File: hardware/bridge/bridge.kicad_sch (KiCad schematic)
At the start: 5 parts, among them U1 SIT3088EEUA

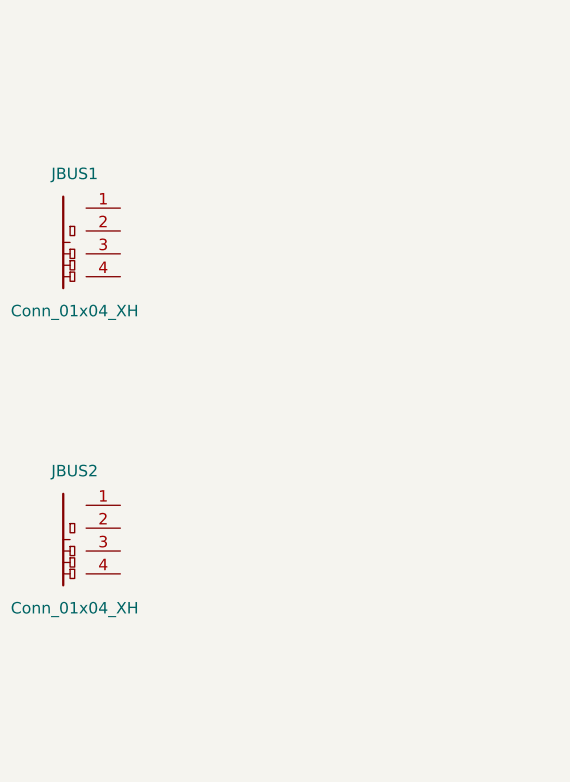
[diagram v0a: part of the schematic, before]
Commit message: hardware: bridge adds DC barrel jacks with reverse-polarity protection
- JDC1, JDC2: JLCPCB C2880546 DC-005K-5A-2.0 barrel jacks (2.0 mm center
  pin, 5.5 mm OD), one per bus connector. Lets the bridge (or any node
  daisy-chained off it) accept a wall-wart input directly instead of
  only bus V+ from another node.
- D1, D2: MBRD10200 Schottky diodes (10 A / 200 V, DPAK, LCSC C260297)
  in series between each DC jack and the corresponding JBUS V+. Protects
  against reverse polarity on the jack and prevents two simultaneously
  plugged jacks from back-feeding each other (diode-OR).

Footprints picked for JLCPCB match:
- DC jack: Connector_BarrelJack:BarrelJack_CUI_PJ-063AH_Horizontal
  (CUI PJ-063AH is 2.0x5.5 mm TH, same electrical spec as DC-005K; close
   mechanical match — verify against datasheet before first fab run)
- Diode:   Package_TO_SOT_SMD:TO-252-2 (DPAK, matches MBRD10200 exactly)

Wiring still pending.
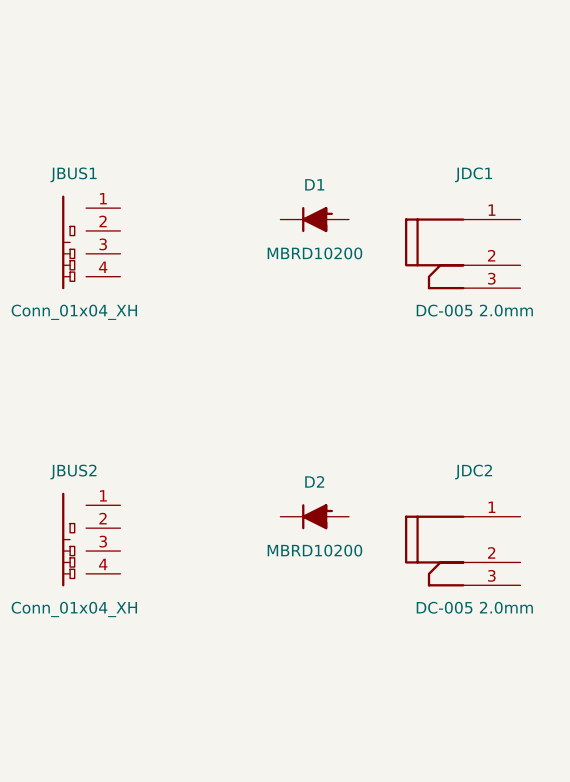
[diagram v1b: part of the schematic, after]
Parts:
- added D1, D2: MBRD10200, Package_TO_SOT_SMD:TO-252-2, symbol Device:D_Schottky
- added JDC1, JDC2: DC-005 2.0mm, Connector_BarrelJack:BarrelJack_CUI_PJ-063AH_Horizontal, symbol Connector:Barrel_Jack_Switch
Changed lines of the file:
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@@
 		(property "Sheetfile" "psu.kicad_sch" (at 25.4 92.0146 0) (effects (font (size 1.27 1.27)) (justify left top)))
+	)
+	(symbol
+		(lib_id "Connector:Barrel_Jack_Switch")
+		(at 228.6 91.44 0)
+		(unit 1)
+		(exclude_from_sim no) (in_bom yes) (on_board yes) (dnp no)
+		(uuid "jdc10001-0000-0000-0000-000000000001")
+		(property "Reference" "JDC1"
+			(at 228.6 83.82 0)
+			(effects (font (size 1.27 1.27)))
+		)
+		(property "Value" "DC-005 2.0mm"
+			(at 228.6 99.06 0)
+			(effects (font (size 1.27 1.27)))
+		)
+		(property "Footprint" "Connector_BarrelJack:BarrelJack_CUI_PJ-063AH_Horizontal"
+			(at 228.6 91.44 0)
+			(effects (font (size 1.27 1.27)) hide)
+		)
+		(property "Datasheet" "~"
+			(at 228.6 91.44 0)
+			(effects (font (size 1.27 1.27)) hide)
+		)
+		(property "Description" "DC barrel jack, 2.0mm center pin, 5A — alternate power input parallel to JBUS1"
+			(at 228.6 91.44 0)
+			(effects (font (size 1.27 1.27)) hide)
+		)
+		(property "LCSC" "C2880546"
+			(at 228.6 91.44 0)
+			(effects (font (size 1.27 1.27)) hide)
+		)
+		(property "MPN" "DC-005K-5A-2.0"
+			(at 228.6 91.44 0)
+			(effects (font (size 1.27 1.27)) hide)
+		)
+		(property "Manufacturer" "XKB Connectivity"
+			(at 228.6 91.44 0)
+			(effects (font (size 1.27 1.27)) hide)
+		)
+		(pin "1" (uuid "jdc10001-0001-0000-0000-000000000001"))
+		(pin "2" (uuid "jdc10001-0002-0000-0000-000000000001"))
+		(pin "3" (uuid "jdc10001-0003-0000-0000-000000000001"))
+		(instances
+			(project "bridge"
+				(path "/c1d2e3f4-a5b6-7890-1234-567890abcdef"
+					(reference "JDC1") (unit 1)
+				)
+			)
+		)
+	)
+	(symbol
+		(lib_id "Device:D_Schottky")
+		(at 210.82 88.9 0)
+		(unit 1)
+		(exclude_from_sim no) (in_bom yes) (on_board yes) (dnp no)
+		(property "Reference" "D1"
+			(at 210.82 85.09 0)
+			(effects (font (size 1.27 1.27)))
+		)
+		(property "Value" "MBRD10200"
+			(at 210.82 92.71 0)
+			(effects (font (size 1.27 1.27)))
+		)
+		(property "Footprint" "Package_TO_SOT_SMD:TO-252-2"
+			(at 210.82 88.9 0)
+			(effects (font (size 1.27 1.27)) hide)
+		)
+		(property "Datasheet" "https://www.onsemi.com/pdf/datasheet/mbrd1035ct-d.pdf"
+			(at 210.82 88.9 0)
+			(effects (font (size 1.27 1.27)) hide)
+		)
+		(property "Description" "Schottky 10A 200V DPAK — reverse polarity on JDC1"
+			(at 210.82 88.9 0)
+			(effects (font (size 1.27 1.27)) hide)
+		)
+		(property "LCSC" "C260297"
+			(at 210.82 88.9 0)
+			(effects (font (size 1.27 1.27)) hide)
+		)
+		(property "MPN" "MBRD10200"
+			(at 210.82 88.9 0)
+			(effects (font (size 1.27 1.27)) hide)
+		)
+		(property "Manufacturer" "onsemi"
+			(at 210.82 88.9 0)
+			(effects (font (size 1.27 1.27)) hide)
+		)
+		(pin "1")
+		(pin "2")
+		(instances
+			(project "bridge"
+				(path "/c1d2e3f4-a5b6-7890-1234-567890abcdef"
+					(reference "D1") (unit 1)
+				)
+			)
+		)
+	)
+	(symbol
+		(lib_id "Connector:Barrel_Jack_Switch")
+		(at 228.6 124.46 0)
+		(unit 1)
+		(exclude_from_sim no) (in_bom yes) (on_board yes) (dnp no)
+		(uuid "jdc20001-0000-0000-0000-000000000002")
+		(property "Reference" "JDC2"
+			(at 228.6 116.84 0)
+			(effects (font (size 1.27 1.27)))
+		)
+		(property "Value" "DC-005 2.0mm"
+			(at 228.6 132.08 0)
+			(effects (font (size 1.27 1.27)))
+		)
+		(property "Footprint" "Connector_BarrelJack:BarrelJack_CUI_PJ-063AH_Horizontal"
+			(at 228.6 124.46 0)
+			(effects (font (size 1.27 1.27)) hide)
+		)
+		(property "Datasheet" "~"
+			(at 228.6 124.46 0)
+			(effects (font (size 1.27 1.27)) hide)
+		)
+		(property "Description" "DC barrel jack, 2.0mm center pin, 5A — alternate power input parallel to JBUS2"
+			(at 228.6 124.46 0)
+			(effects (font (size 1.27 1.27)) hide)
+		)
+		(property "LCSC" "C2880546"
+			(at 228.6 124.46 0)
+			(effects (font (size 1.27 1.27)) hide)
+		)
+		(property "MPN" "DC-005K-5A-2.0"
+			(at 228.6 124.46 0)
+			(effects (font (size 1.27 1.27)) hide)
+		)
+		(property "Manufacturer" "XKB Connectivity"
+			(at 228.6 124.46 0)
+			(effects (font (size 1.27 1.27)) hide)
+		)
+		(pin "1" (uuid "jdc20001-0001-0000-0000-000000000002"))
+		(pin "2" (uuid "jdc20001-0002-0000-0000-000000000002"))
+		(pin "3" (uuid "jdc20001-0003-0000-0000-000000000002"))
+		(instances
+			(project "bridge"
+				(path "/c1d2e3f4-a5b6-7890-1234-567890abcdef"
+					(reference "JDC2") (unit 1)
+				)
+			)
+		)
+	)
+	(symbol
+		(lib_id "Device:D_Schottky")
+		(at 210.82 121.92 0)
+		(unit 1)
+		(exclude_from_sim no) (in_bom yes) (on_board yes) (dnp no)
+		(property "Reference" "D2"
+			(at 210.82 118.11 0)
+			(effects (font (size 1.27 1.27)))
+		)
+		(property "Value" "MBRD10200"
+			(at 210.82 125.73 0)
+			(effects (font (size 1.27 1.27)))
+		)
+		(property "Footprint" "Package_TO_SOT_SMD:TO-252-2"
+			(at 210.82 121.92 0)
+			(effects (font (size 1.27 1.27)) hide)
+		)
+		(property "Datasheet" "https://www.onsemi.com/pdf/datasheet/mbrd1035ct-d.pdf"
+			(at 210.82 121.92 0)
+			(effects (font (size 1.27 1.27)) hide)
+		)
+		(property "Description" "Schottky 10A 200V DPAK — reverse polarity on JDC2"
+			(at 210.82 121.92 0)
+			(effects (font (size 1.27 1.27)) hide)
+		)
+		(property "LCSC" "C260297"
+			(at 210.82 121.92 0)
+			(effects (font (size 1.27 1.27)) hide)
+		)
+		(property "MPN" "MBRD10200"
+			(at 210.82 121.92 0)
+			(effects (font (size 1.27 1.27)) hide)
+		)
+		(property "Manufacturer" "onsemi"
+			(at 210.82 121.92 0)
+			(effects (font (size 1.27 1.27)) hide)
+		)
+		(pin "1")
+		(pin "2")
+		(instances
+			(project "bridge"
+				(path "/c1d2e3f4-a5b6-7890-1234-567890abcdef"
+					(reference "D2") (unit 1)
+				)
+			)
+		)
 	)
 	(sheet_instances

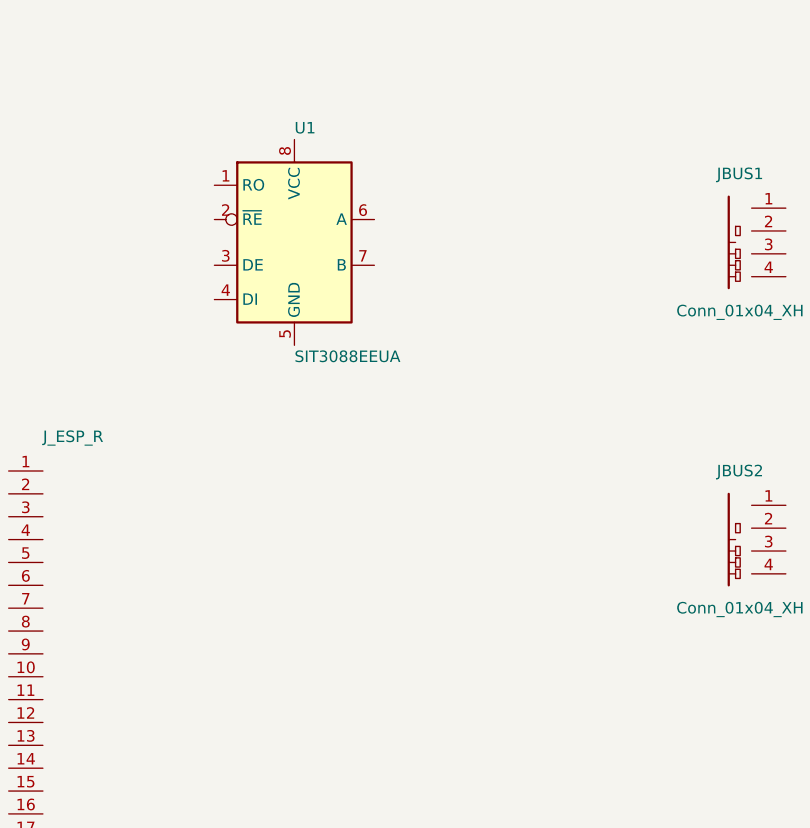
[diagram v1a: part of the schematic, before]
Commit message: hardware: bridge now has two independent RS-485 buses with termination
- Add second SIT3088EEUA transceiver (U3) for Bus 2, parallel to U1
- Add 120 Ω 1206 termination resistors R4/R5 (LCSC C114928) in series
  with solder jumpers JPTERM1/JPTERM2 (normally open). Solder closed at
  each bus endpoint.
- Update docs/README.md: block overview table now lists both transceivers
  and both terminations; power diagram shows the per-bus OR of DC jack +
  bus V+ feeding a common LMR38020 rail
- Add recommended ESP32 pinout for dual-bus operation:
    Bus 1 on UART2 default pins (GPIO 17 TX / 16 RX / 4 DE)
    Bus 2 on UART1 remapped  (GPIO 25 TX / 26 RX / 27 DE)
  UART1 defaults to GPIO 9/10 which collide with SPI flash on most
  ESP32 modules — remap mandatory.
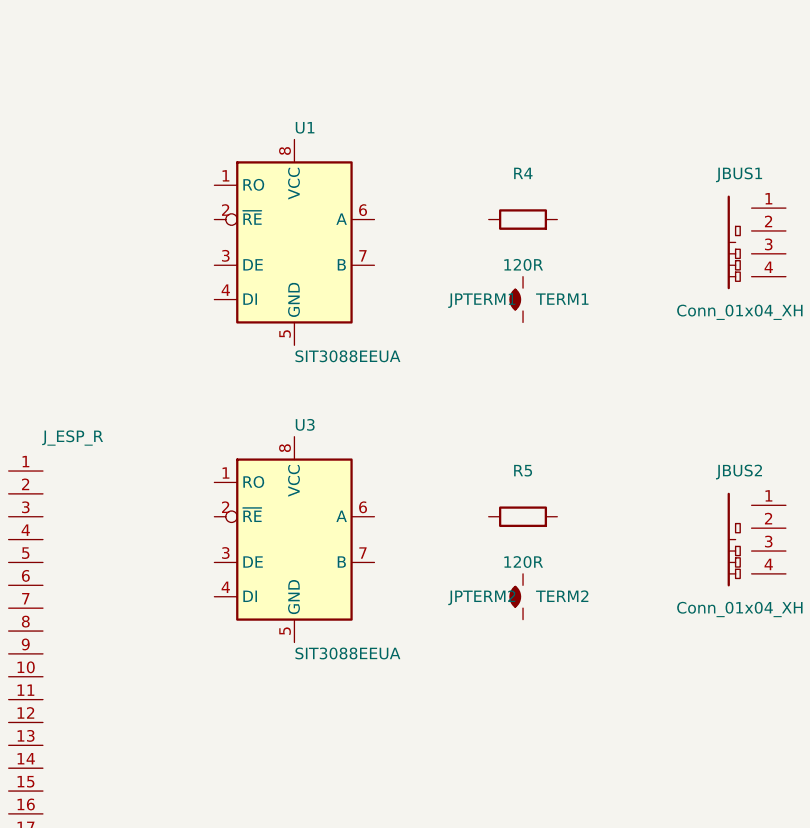
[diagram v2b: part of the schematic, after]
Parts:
- added JPTERM1: TERM1, Jumper:SolderJumper-2_P1.3mm_Open_Pad1.0x1.5mm, symbol Jumper:SolderJumper_2_Open
- added JPTERM2: TERM2, Jumper:SolderJumper-2_P1.3mm_Open_Pad1.0x1.5mm, symbol Jumper:SolderJumper_2_Open
- added R4, R5: 120R, Resistor_SMD:R_1206_3216Metric, symbol Device:R
- added U3: SIT3088EEUA, Package_SO:MSOP-8_3x3mm_P0.65mm, symbol tsumikoro:SIT3088EEUA
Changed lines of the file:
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@@
 		)
+	)
+	(symbol
+		(lib_id "tsumikoro:SIT3088EEUA")
+		(at 134.62 124.46 0)
+		(unit 1)
+		(exclude_from_sim no) (in_bom yes) (on_board yes) (dnp no)
+		(uuid "u3000001-0000-0000-0000-000000000003")
+		(property "Reference" "U3" (at 134.62 111.76 0) (effects (font (size 1.27 1.27)) (justify left)))
+		(property "Value" "SIT3088EEUA" (at 134.62 137.16 0) (effects (font (size 1.27 1.27)) (justify left)))
+		(property "Footprint" "Package_SO:MSOP-8_3x3mm_P0.65mm" (at 134.62 124.46 0) (effects (font (size 1.27 1.27)) hide))
+		(property "Datasheet" "https://www.lcsc.com/datasheet/lcsc_datasheet_2403271503_3PEAK-SIT3088EEUA_C2922535.pdf" (at 134.62 124.46 0) (effects (font (size 1.27 1.27)) hide))
+		(property "Description" "RS-485 Half-Duplex Transceiver — Bus 2" (at 134.62 124.46 0) (effects (font (size 1.27 1.27)) hide))
+		(property "LCSC" "C2922535" (at 134.62 124.46 0) (effects (font (size 1.27 1.27)) hide))
+		(property "MPN" "SIT3088EEUA" (at 134.62 124.46 0) (effects (font (size 1.27 1.27)) hide))
+		(property "Manufacturer" "3PEAK" (at 134.62 124.46 0) (effects (font (size 1.27 1.27)) hide))
+		(pin "1" (uuid "u3000001-0001-0000-0000-000000000003"))
+		(pin "2" (uuid "u3000001-0002-0000-0000-000000000003"))
+		(pin "3" (uuid "u3000001-0003-0000-0000-000000000003"))
+		(pin "4" (uuid "u3000001-0004-0000-0000-000000000003"))
+		(pin "5" (uuid "u3000001-0005-0000-0000-000000000003"))
+		(pin "6" (uuid "u3000001-0006-0000-0000-000000000003"))
+		(pin "7" (uuid "u3000001-0007-0000-0000-000000000003"))
+		(pin "8" (uuid "u3000001-0008-0000-0000-000000000003"))
+		(instances (project "bridge" (path "/c1d2e3f4-a5b6-7890-1234-567890abcdef" (reference "U3") (unit 1))))
+	)
+	(symbol
+		(lib_id "Device:R")
+		(at 160.02 88.9 90)
+		(unit 1)
+		(exclude_from_sim no) (in_bom yes) (on_board yes) (dnp no)
+		(uuid "r4000001-0000-0000-0000-000000000004")
+		(property "Reference" "R4" (at 160.02 83.82 90) (effects (font (size 1.27 1.27))))
+		(property "Value" "120R" (at 160.02 93.98 90) (effects (font (size 1.27 1.27))))
+		(property "Footprint" "Resistor_SMD:R_1206_3216Metric" (at 160.02 88.9 0) (effects (font (size 1.27 1.27)) hide))
+		(property "Datasheet" "~" (at 160.02 88.9 0) (effects (font (size 1.27 1.27)) hide))
+		(property "Description" "Bus 1 termination 120R 1% 1206 (series with JPTERM1)" (at 160.02 88.9 0) (effects (font (size 1.27 1.27)) hide))
+		(property "LCSC" "C114928" (at 160.02 88.9 0) (effects (font (size 1.27 1.27)) hide))
+		(property "MPN" "RC1206FR-07120RL" (at 160.02 88.9 0) (effects (font (size 1.27 1.27)) hide))
+		(property "Manufacturer" "Yageo" (at 160.02 88.9 0) (effects (font (size 1.27 1.27)) hide))
+		(pin "1" (uuid "r4000001-0001-0000-0000-000000000004"))
+		(pin "2" (uuid "r4000001-0002-0000-0000-000000000004"))
+		(instances (project "bridge" (path "/c1d2e3f4-a5b6-7890-1234-567890abcdef" (reference "R4") (unit 1))))
+	)
+	(symbol
+		(lib_id "Jumper:SolderJumper_2_Open")
+		(at 160.02 97.79 90)
+		(unit 1)
+		(exclude_from_sim no) (in_bom yes) (on_board yes) (dnp no)
+		(uuid "jpterm01-0000-0000-0000-000000000001")
+		(property "Reference" "JPTERM1" (at 155.575 97.79 90) (effects (font (size 1.27 1.27))))
+		(property "Value" "TERM1" (at 164.465 97.79 90) (effects (font (size 1.27 1.27))))
+		(property "Footprint" "Jumper:SolderJumper-2_P1.3mm_Open_Pad1.0x1.5mm" (at 160.02 97.79 0) (effects (font (size 1.27 1.27)) hide))
+		(property "Datasheet" "~" (at 160.02 97.79 0) (effects (font (size 1.27 1.27)) hide))
+		(property "Description" "Bus 1 termination enable (normally open)" (at 160.02 97.79 0) (effects (font (size 1.27 1.27)) hide))
+		(pin "1" (uuid "jpterm01-0001-0000-0000-000000000001"))
+		(pin "2" (uuid "jpterm01-0002-0000-0000-000000000001"))
+		(instances (project "bridge" (path "/c1d2e3f4-a5b6-7890-1234-567890abcdef" (reference "JPTERM1") (unit 1))))
+	)
+	(symbol
+		(lib_id "Device:R")
+		(at 160.02 121.92 90)
+		(unit 1)
+		(exclude_from_sim no) (in_bom yes) (on_board yes) (dnp no)
+		(uuid "r5000001-0000-0000-0000-000000000005")
+		(property "Reference" "R5" (at 160.02 116.84 90) (effects (font (size 1.27 1.27))))
+		(property "Value" "120R" (at 160.02 127 90) (effects (font (size 1.27 1.27))))
+		(property "Footprint" "Resistor_SMD:R_1206_3216Metric" (at 160.02 121.92 0) (effects (font (size 1.27 1.27)) hide))
+		(property "Datasheet" "~" (at 160.02 121.92 0) (effects (font (size 1.27 1.27)) hide))
+		(property "Description" "Bus 2 termination 120R 1% 1206 (series with JPTERM2)" (at 160.02 121.92 0) (effects (font (size 1.27 1.27)) hide))
+		(property "LCSC" "C114928" (at 160.02 121.92 0) (effects (font (size 1.27 1.27)) hide))
+		(property "MPN" "RC1206FR-07120RL" (at 160.02 121.92 0) (effects (font (size 1.27 1.27)) hide))
+		(property "Manufacturer" "Yageo" (at 160.02 121.92 0) (effects (font (size 1.27 1.27)) hide))
+		(pin "1" (uuid "r5000001-0001-0000-0000-000000000005"))
+		(pin "2" (uuid "r5000001-0002-0000-0000-000000000005"))
+		(instances (project "bridge" (path "/c1d2e3f4-a5b6-7890-1234-567890abcdef" (reference "R5") (unit 1))))
+	)
+	(symbol
+		(lib_id "Jumper:SolderJumper_2_Open")
+		(at 160.02 130.81 90)
+		(unit 1)
+		(exclude_from_sim no) (in_bom yes) (on_board yes) (dnp no)
+		(uuid "jpterm02-0000-0000-0000-000000000002")
+		(property "Reference" "JPTERM2" (at 155.575 130.81 90) (effects (font (size 1.27 1.27))))
+		(property "Value" "TERM2" (at 164.465 130.81 90) (effects (font (size 1.27 1.27))))
+		(property "Footprint" "Jumper:SolderJumper-2_P1.3mm_Open_Pad1.0x1.5mm" (at 160.02 130.81 0) (effects (font (size 1.27 1.27)) hide))
+		(property "Datasheet" "~" (at 160.02 130.81 0) (effects (font (size 1.27 1.27)) hide))
+		(property "Description" "Bus 2 termination enable (normally open)" (at 160.02 130.81 0) (effects (font (size 1.27 1.27)) hide))
+		(pin "1" (uuid "jpterm02-0001-0000-0000-000000000002"))
+		(pin "2" (uuid "jpterm02-0002-0000-0000-000000000002"))
+		(instances (project "bridge" (path "/c1d2e3f4-a5b6-7890-1234-567890abcdef" (reference "JPTERM2") (unit 1))))
 	)
 	(sheet_instances
